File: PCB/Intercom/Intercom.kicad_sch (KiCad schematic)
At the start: 73 parts, among them J1 Reset, J2 JST-PH-SM4-TB, J4 TC2030-USB-NL-DS, J5 USB-C-Socket-H, P1 Square, P2 Square, SW1 SW_SPST, U1 MD8942, U2 ESP32-S3-MINI-1, U4 ICS43434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

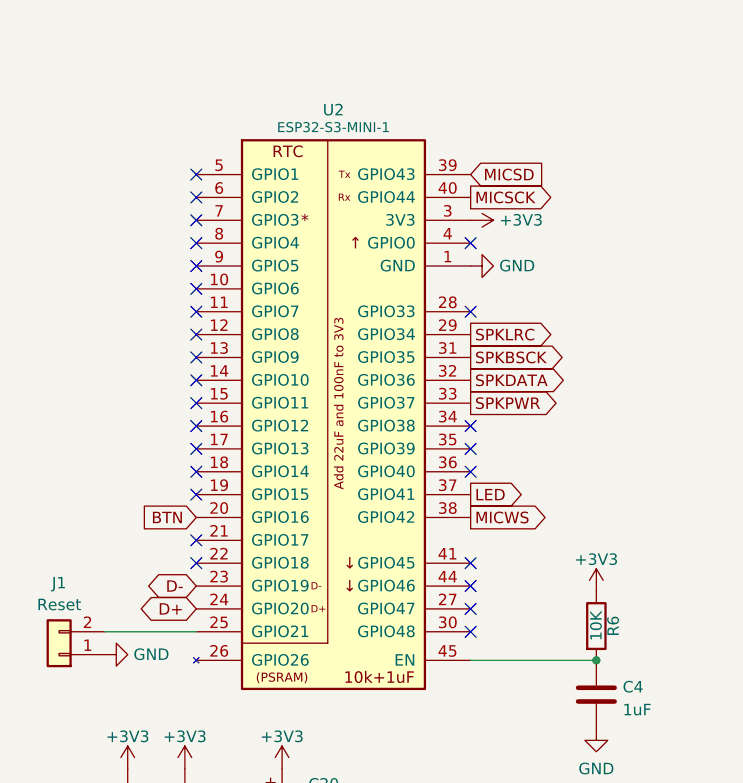
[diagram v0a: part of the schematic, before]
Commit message: Power control for LEDs
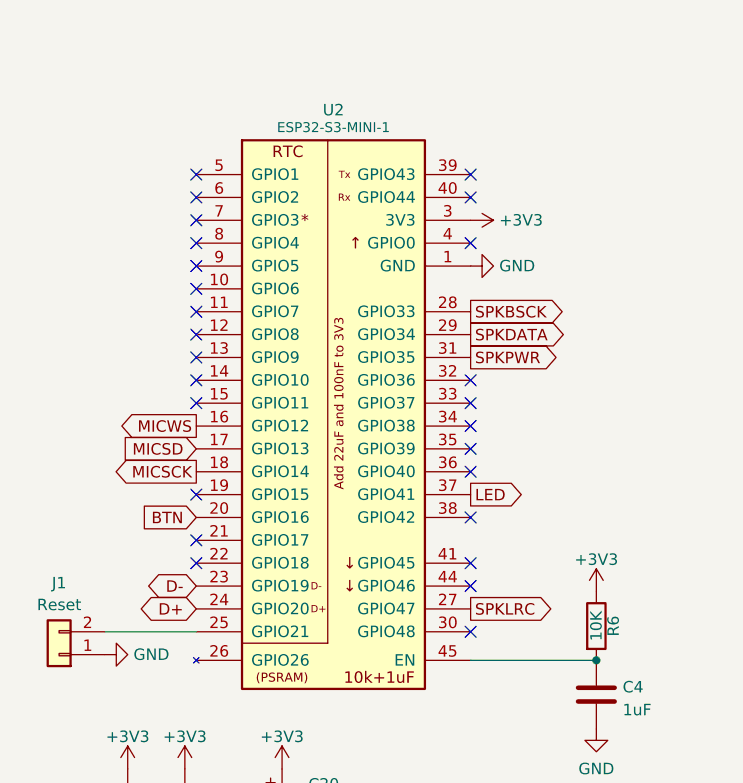
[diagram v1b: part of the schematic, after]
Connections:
- net MICSCK: now also U2.18 (GPIO14); no longer U2.40 (GPIO44)
- net MICSD: now also U2.17 (GPIO13); no longer U2.39 (GPIO43)
- net MICWS: now also U2.16 (GPIO12); no longer U2.38 (GPIO42)
- net SPKBSCK: now also U2.28 (GPIO33); no longer U2.31 (GPIO35)
- net SPKDATA: now also U2.29 (GPIO34); no longer U2.32 (GPIO36)
- net SPKLRC: now also U2.27 (GPIO47); no longer U2.29 (GPIO34)
- net SPKPWR: now also U2.31 (GPIO35); no longer U2.33 (GPIO37)
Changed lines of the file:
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@@
 	)
 	(no_connect
-		(at 35.56 83.82)
+		(at 66.04 53.34)
 	)
 	(no_connect
@@
 	)
 	(no_connect
-		(at 35.56 81.28)
+		(at 66.04 50.8)
 	)
 	(no_connect
@@
 	)
 	(no_connect
-		(at 66.04 66.04)
+		(at 66.04 73.66)
 	)
 	(no_connect
@@
 	)
 	(no_connect
-		(at 35.56 78.74)
+		(at 66.04 88.9)
 	)
 	(no_connect
@@
 	)
 	(no_connect
-		(at 66.04 99.06)
+		(at 66.04 76.2)
 	)
 	(no_connect
@@
 	(global_label "MICSCK"
 		(shape output)
-		(at 66.04 53.34 0)
-		(fields_autoplaced yes)
-		(effects
-			(font
-				(size 1.27 1.27)
-			)
-			(justify left)
-		)
-		(property "Intersheetrefs" "${INTERSHEET_REFS}"
-			(at 75.4467 53.34 0)
-			(effects
-				(font
-					(size 1.27 1.27)
-				)
-				(justify left)
+		(at 35.56 83.82 180)
+		(fields_autoplaced yes)
+		(effects
+			(font
+				(size 1.27 1.27)
+			)
+			(justify right)
+		)
+		(property "Intersheetrefs" "${INTERSHEET_REFS}"
+			(at 26.1533 83.82 0)
+			(effects
+				(font
+					(size 1.27 1.27)
+				)
+				(justify right)
 				(hide yes)
 			)
@@
 	(global_label "SPKDATA"
 		(shape output)
-		(at 66.04 73.66 0)
+		(at 66.04 68.58 0)
 		(fields_autoplaced yes)
 		(effects
@@
 		)
 		(property "Intersheetrefs" "${INTERSHEET_REFS}"
-			(at 76.5353 73.66 0)
+			(at 76.5353 68.58 0)
 			(effects
 				(font
@@
 	(global_label "SPKBSCK"
 		(shape output)
-		(at 66.04 71.12 0)
+		(at 66.04 66.04 0)
 		(fields_autoplaced yes)
 		(effects
@@
 		)
 		(property "Intersheetrefs" "${INTERSHEET_REFS}"
-			(at 77.14 71.12 0)
+			(at 77.14 66.04 0)
 			(effects
 				(font
@@
 	(global_label "SPKPWR"
 		(shape output)
-		(at 66.04 76.2 0)
+		(at 66.04 71.12 0)
 		(fields_autoplaced yes)
 		(effects
@@
 		)
 		(property "Intersheetrefs" "${INTERSHEET_REFS}"
-			(at 76.1119 76.2 0)
+			(at 76.1119 71.12 0)
 			(effects
 				(font
@@
 	(global_label "MICSD"
 		(shape input)
-		(at 66.04 50.8 0)
-		(fields_autoplaced yes)
-		(effects
-			(font
-				(size 1.27 1.27)
-			)
-			(justify left)
-		)
-		(property "Intersheetrefs" "${INTERSHEET_REFS}"
-			(at 74.1767 50.8 0)
-			(effects
-				(font
-					(size 1.27 1.27)
-				)
-				(justify left)
+		(at 35.56 81.28 180)
+		(fields_autoplaced yes)
+		(effects
+			(font
+				(size 1.27 1.27)
+			)
+			(justify right)
+		)
+		(property "Intersheetrefs" "${INTERSHEET_REFS}"
+			(at 27.4233 81.28 0)
+			(effects
+				(font
+					(size 1.27 1.27)
+				)
+				(justify right)
 				(hide yes)
 			)
@@
 	(global_label "MICWS"
 		(shape output)
-		(at 66.04 88.9 0)
-		(fields_autoplaced yes)
-		(effects
-			(font
-				(size 1.27 1.27)
-			)
-			(justify left)
-		)
-		(property "Intersheetrefs" "${INTERSHEET_REFS}"
-			(at 74.3581 88.9 0)
-			(effects
-				(font
-					(size 1.27 1.27)
-				)
-				(justify left)
+		(at 35.56 78.74 180)
+		(fields_autoplaced yes)
+		(effects
+			(font
+				(size 1.27 1.27)
+			)
+			(justify right)
+		)
+		(property "Intersheetrefs" "${INTERSHEET_REFS}"
+			(at 27.2419 78.74 0)
+			(effects
+				(font
+					(size 1.27 1.27)
+				)
+				(justify right)
 				(hide yes)
 			)
@@
 	(global_label "SPKLRC"
 		(shape output)
-		(at 66.04 68.58 0)
+		(at 66.04 99.06 0)
 		(fields_autoplaced yes)
 		(effects
@@
 		)
 		(property "Intersheetrefs" "${INTERSHEET_REFS}"
-			(at 75.6886 68.58 0)
-			(effects
-				(font
+			(at 75.6886 99.06 0)
+			(effects
+				(font
